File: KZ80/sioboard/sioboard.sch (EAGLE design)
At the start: 18 parts, among them J1 CLKSEL

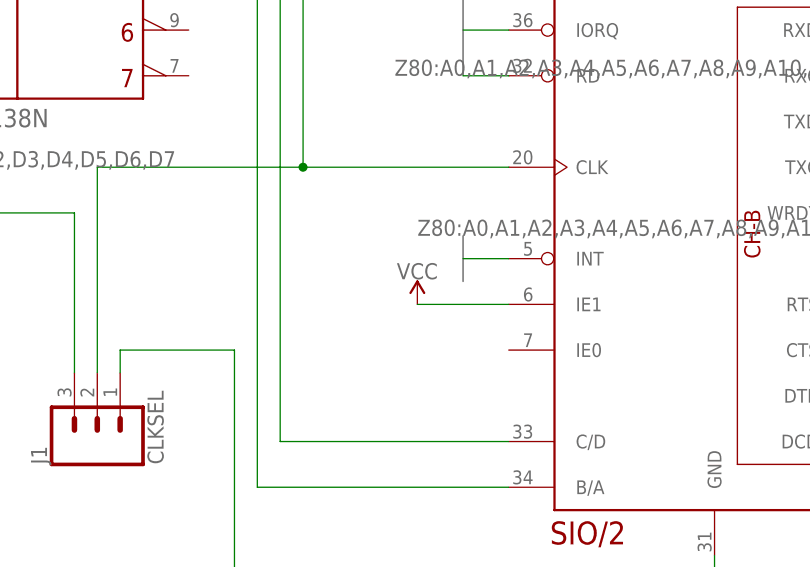
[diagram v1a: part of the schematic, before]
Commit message: sioboard: break out interrupt priority pins.
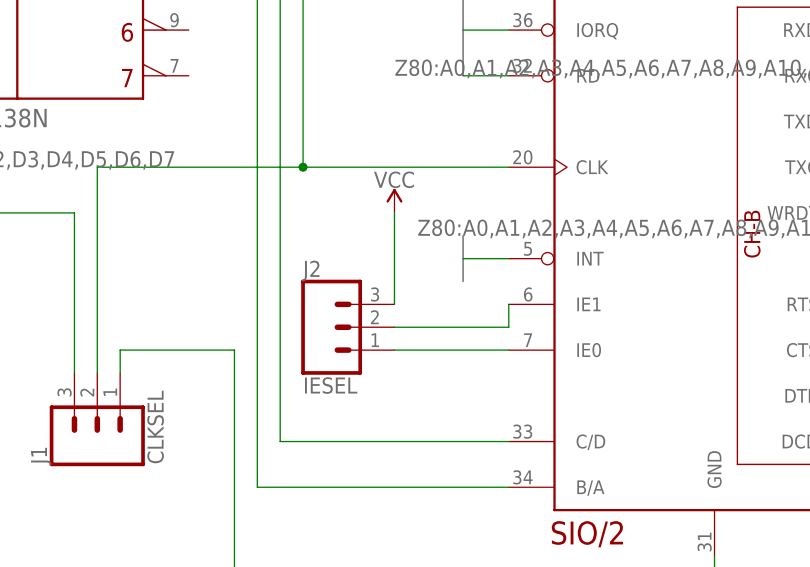
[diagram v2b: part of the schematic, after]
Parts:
- added J2: IESEL, SparkFun-Connectors:CONN_03
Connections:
- new net N$25: J2.1, U$2.IE0
- new net N$26: J2.2, U$2.IE1
- net VCC: now also J2.3; no longer U$2.IE1
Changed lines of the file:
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@@
 </variantdefs>
 <classes>
-<class number="0" name="default" width="0.2032" drill="0.4064">
-<clearance class="0" value="0.2032"/>
+<class number="0" name="default" width="0.1524" drill="0.254">
+<clearance class="0" value="0.1524"/>
 </class>
 </classes>
@@
 <part name="SUPPLY9" library="SparkFun-PowerSymbols" deviceset="VCC" device=""/>
 <part name="GND11" library="SparkFun-PowerSymbols" deviceset="GND" device=""/>
+<part name="J2" library="SparkFun-Connectors" deviceset="CONN_03" device="" value="IESEL"/>
 </parts>
 <sheets>
@@
 <attribute name="VALUE" x="58.42" y="28.194" size="1.778" layer="96" align="bottom-center"/>
 </instance>
-<instance part="SUPPLY4" gate="G$1" x="114.3" y="-15.24" smashed="yes">
-<attribute name="VALUE" x="114.3" y="-12.446" size="1.778" layer="96" align="bottom-center"/>
+<instance part="SUPPLY4" gate="G$1" x="111.76" y="-5.08" smashed="yes">
+<attribute name="VALUE" x="111.76" y="-2.286" size="1.778" layer="96" align="bottom-center"/>
 </instance>
 <instance part="V2" gate="/1" x="76.2" y="68.58" smashed="yes">
@@
 <instance part="GND11" gate="1" x="-17.78" y="30.48" smashed="yes">
 <attribute name="VALUE" x="-17.78" y="30.226" size="1.778" layer="96" align="top-center"/>
+</instance>
+<instance part="J2" gate="J$1" x="104.14" y="-17.78" smashed="yes">
+<attribute name="VALUE" x="101.6" y="-25.146" size="1.778" layer="96" font="vector"/>
+<attribute name="NAME" x="101.6" y="-12.192" size="1.778" layer="95" font="vector"/>
 </instance>
 </instances>
@@
 </segment>
 <segment>
-<pinref part="SUPPLY4" gate="G$1" pin="VCC"/>
-<pinref part="U$2" gate="G$1" pin="IE1"/>
-<wire x1="114.3" y1="-15.24" x2="124.46" y2="-15.24" width="0.1524" layer="91"/>
-</segment>
-<segment>
 <pinref part="V2" gate="/+UB" pin="+UB"/>
 <pinref part="SUPPLY5" gate="G$1" pin="VCC"/>
@@
 <pinref part="C4" gate="G$1" pin="1"/>
 <wire x1="-17.78" y1="45.72" x2="-17.78" y2="43.18" width="0.1524" layer="91"/>
+</segment>
+<segment>
+<pinref part="SUPPLY4" gate="G$1" pin="VCC"/>
+<pinref part="J2" gate="J$1" pin="3"/>
+<wire x1="111.76" y1="-5.08" x2="111.76" y2="-15.24" width="0.1524" layer="91"/>
 </segment>
 </net>
@@
 </segment>
 </net>
+<net name="N$25" class="0">
+<segment>
+<pinref part="J2" gate="J$1" pin="1"/>
+<pinref part="U$2" gate="G$1" pin="IE0"/>
+<wire x1="111.76" y1="-20.32" x2="124.46" y2="-20.32" width="0.1524" layer="91"/>
+</segment>
+</net>
+<net name="N$26" class="0">
+<segment>
+<pinref part="J2" gate="J$1" pin="2"/>
+<wire x1="111.76" y1="-17.78" x2="124.46" y2="-17.78" width="0.1524" layer="91"/>
+<pinref part="U$2" gate="G$1" pin="IE1"/>
+<wire x1="124.46" y1="-17.78" x2="124.46" y2="-15.24" width="0.1524" layer="91"/>
+</segment>
+</net>
